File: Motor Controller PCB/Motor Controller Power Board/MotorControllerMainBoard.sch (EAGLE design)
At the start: 51 parts, among them U1 CDBA340L-G

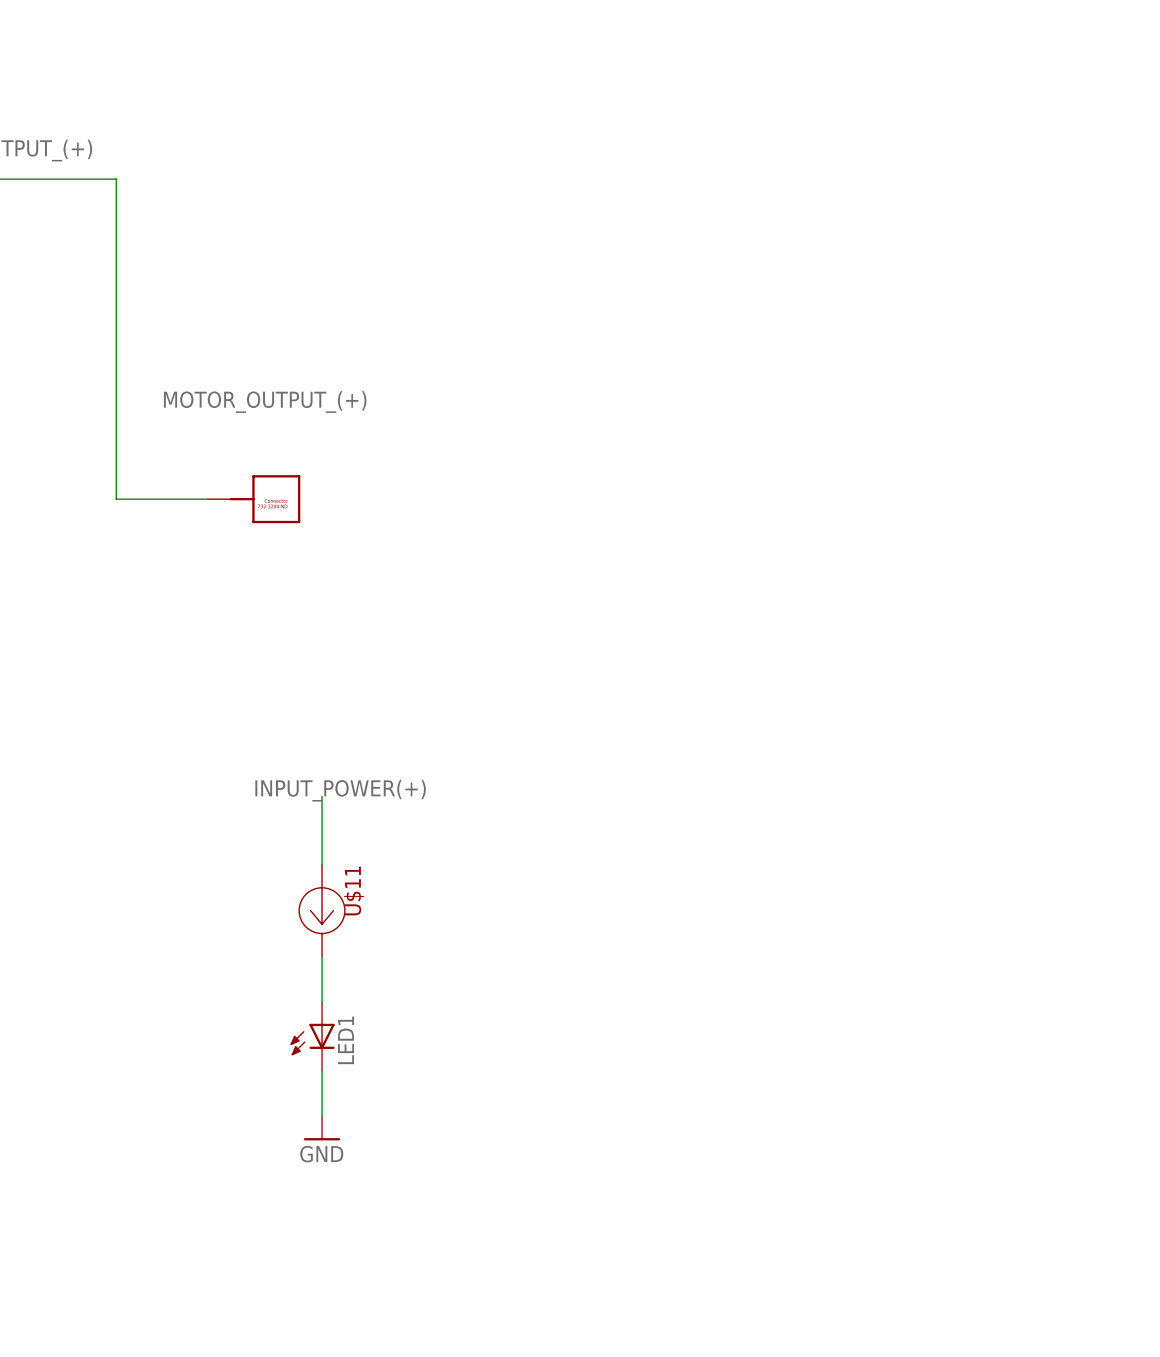
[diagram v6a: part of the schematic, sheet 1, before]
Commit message: Added headers, selected resistor for fet driver
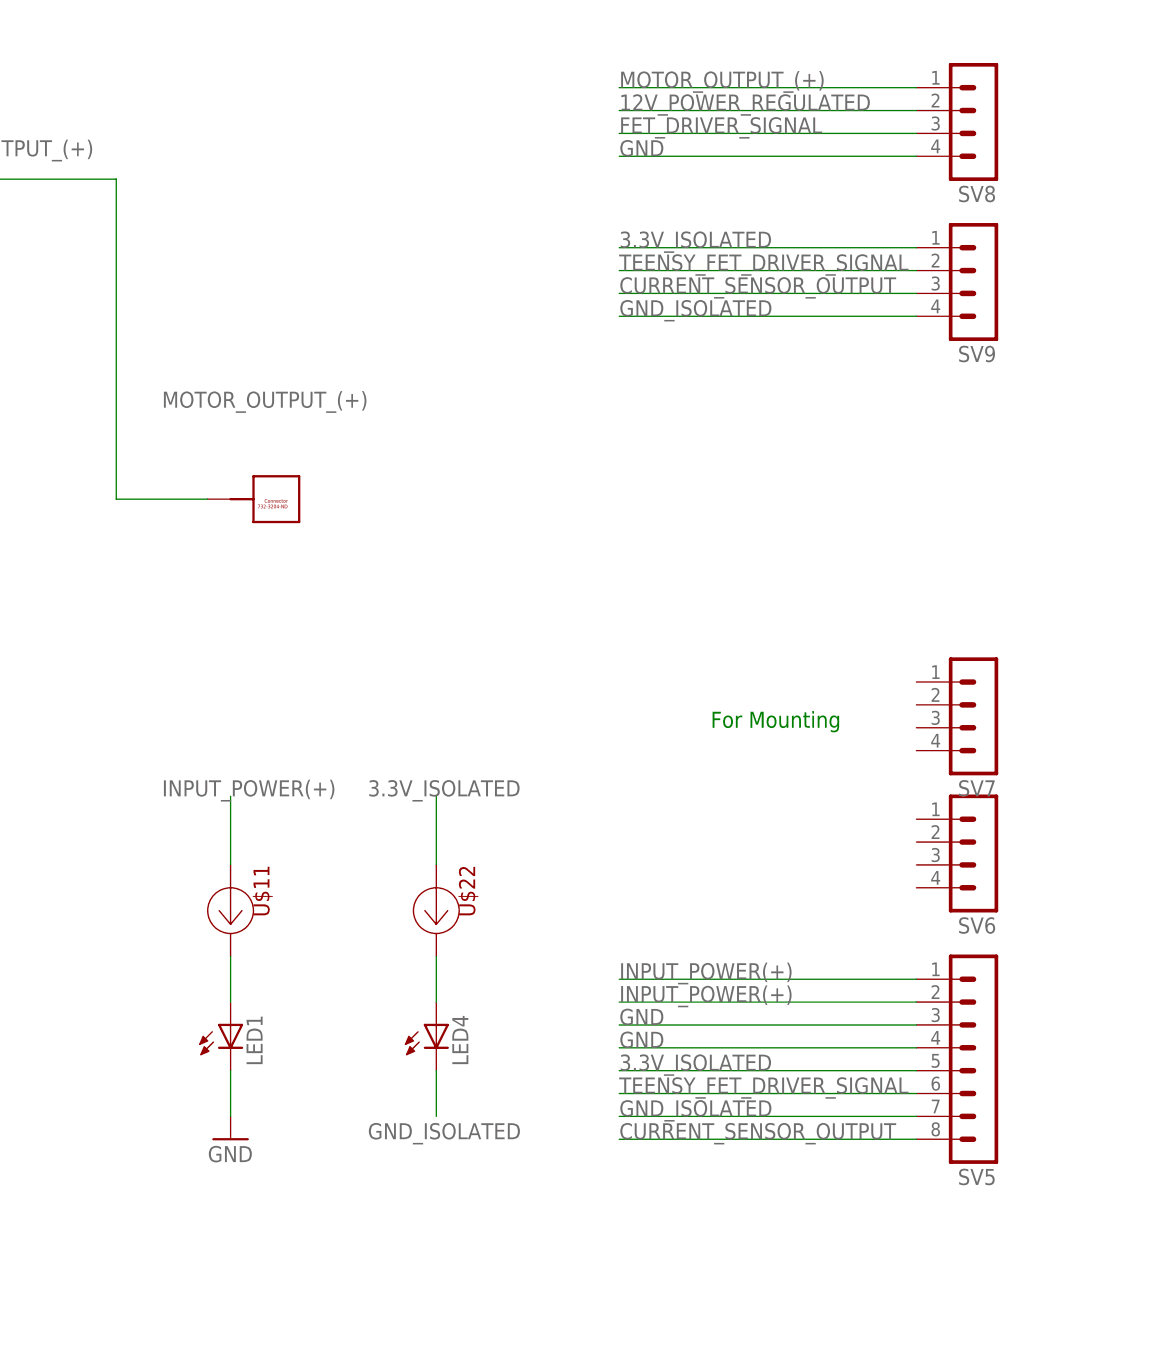
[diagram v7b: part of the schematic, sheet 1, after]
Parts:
- added LED4: (no value), led:LEDCHIPLED_1206
- added SV5: (no value), con-lstb:MA08-1
- added SV6, SV7, SV8, SV9: (no value), con-lstb:MA04-1
- added U$22: (no value), MotorControllerEagleLibrary:AL5809-20S1-7
- R1: value 4.7k -> 332
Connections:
- removed net 3.3V_POWER_REGULATED: L1.1, LED3.A
- new net 3.3V_ISOLATED: L1.1, LED3.A, SV5.5, SV9.1, U$22.A
- new net N$14: LED4.A, U$22.C
- new net TEENSY_FET_DRIVER_SIGNAL: SV5.6, SV9.2
- net 12V_POWER_REGULATED: now also SV8.2
- net CURRENT_SENSOR_OUTPUT: now also SV5.8, SV9.3
- net FET_DRIVER_SIGNAL: now also SV8.3
- net GND: now also SV5.3, SV5.4, SV8.4
- net GND_ISOLATED: now also LED4.C, SV5.7, SV9.4
- net INPUT_POWER(+): now also SV5.1, SV5.2
- net MOTOR_OUTPUT_(+): now also SV8.1
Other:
- note added: "For Mounting"
- note added: "~4mA to 6mA (LED Vf 1.5V to 1.9V) maximum 8mA minimum 2mA"
- note removed: "This component needs to be spec'ed"
- moved on the sheet: LED1, U$11
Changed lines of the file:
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@@
 <part name="FRAME3" library="E-P-008-R1.2" deviceset="FRAME_A_L" device=""/>
 <part name="FRAME4" library="E-P-008-R1.2" deviceset="FRAME_A_L" device=""/>
-<part name="R1" library="resistor" library_urn="urn:adsk.eagle:library:348" deviceset="R-US_" device="R0805" package3d_urn="urn:adsk.eagle:package:26059/1" value="4.7k"/>
+<part name="R1" library="resistor" library_urn="urn:adsk.eagle:library:348" deviceset="R-US_" device="R0805" package3d_urn="urn:adsk.eagle:package:26059/1" value="332"/>
 <part name="C1" library="rcl" library_urn="urn:adsk.eagle:library:334" deviceset="C-EU" device="C1210" package3d_urn="urn:adsk.eagle:package:23619/2" value="22uF"/>
 <part name="C2" library="rcl" library_urn="urn:adsk.eagle:library:334" deviceset="C-EU" device="C0805" package3d_urn="urn:adsk.eagle:package:23617/2" value="2.2uF"/>
@@
 <part name="LED3" library="SparkFun (2015_10_14 22_27_04 UTC)" deviceset="LED" device="1206"/>
 <part name="U$21" library="MotorControllerEagleLibrary" deviceset="AL5809-20S1-7" device=""/>
+<part name="SV5" library="con-lstb" library_urn="urn:adsk.eagle:library:162" deviceset="MA08-1" device="" package3d_urn="urn:adsk.eagle:package:8343/1"/>
+<part name="SV6" library="con-lstb" library_urn="urn:adsk.eagle:library:162" deviceset="MA04-1" device="" package3d_urn="urn:adsk.eagle:package:8337/1"/>
+<part name="SV7" library="con-lstb" library_urn="urn:adsk.eagle:library:162" deviceset="MA04-1" device="" package3d_urn="urn:adsk.eagle:package:8337/1"/>
+<part name="SV8" library="con-lstb" library_urn="urn:adsk.eagle:library:162" deviceset="MA04-1" device="" package3d_urn="urn:adsk.eagle:package:8337/1"/>
+<part name="SV9" library="con-lstb" library_urn="urn:adsk.eagle:library:162" deviceset="MA04-1" device="" package3d_urn="urn:adsk.eagle:package:8337/1"/>
+<part name="U$22" library="MotorControllerEagleLibrary" deviceset="AL5809-20S1-7" device=""/>
+<part name="LED4" library="led" library_urn="urn:adsk.eagle:library:259" deviceset="LED" device="CHIPLED_1206" package3d_urn="urn:adsk.eagle:package:15823/1"/>
 </parts>
 <sheets>
@@
 <text x="175.26" y="25.4" size="2.286" layer="94">Keep it looking neat. Use other sheets to make complicated circuits</text>
 <text x="20.32" y="58.42" size="1.778" layer="91">Terminal Block (Negative)</text>
+<text x="236.22" y="121.92" size="1.778" layer="91">For Mounting</text>
 </plain>
 <instances>
@@
 <instance part="U$15" gate="G$1" x="187.96" y="147.32" rot="R180"/>
 <instance part="U$16" gate="G$1" x="15.24" y="106.68"/>
-<instance part="U$11" gate="G$1" x="193.04" y="101.6" rot="R180"/>
-<instance part="LED1" gate="G$1" x="193.04" y="88.9"/>
-<instance part="GND22" gate="1" x="193.04" y="76.2"/>
+<instance part="U$11" gate="G$1" x="182.88" y="101.6" rot="R180"/>
+<instance part="LED1" gate="G$1" x="182.88" y="88.9"/>
+<instance part="GND22" gate="1" x="182.88" y="76.2"/>
+<instance part="SV5" gate="1" x="266.7" y="86.36" rot="R180"/>
+<instance part="SV6" gate="1" x="266.7" y="106.68" rot="R180"/>
+<instance part="SV7" gate="1" x="266.7" y="121.92" rot="R180"/>
+<instance part="SV8" gate="1" x="266.7" y="187.96" rot="R180"/>
+<instance part="SV9" gate="1" x="266.7" y="170.18" rot="R180"/>
+<instance part="U$22" gate="G$1" x="205.74" y="101.6" rot="R180"/>
+<instance part="LED4" gate="G$1" x="205.74" y="88.9"/>
 </instances>
 <busses>
@@
 </segment>
 <segment>
-<wire x1="193.04" y1="114.3" x2="193.04" y2="106.68" width="0.1524" layer="91"/>
+<wire x1="182.88" y1="114.3" x2="182.88" y2="106.68" width="0.1524" layer="91"/>
 <pinref part="U$11" gate="G$1" pin="A"/>
-<label x="185.42" y="114.3" size="1.778" layer="95"/>
+<label x="175.26" y="114.3" size="1.778" layer="95"/>
+</segment>
+<segment>
+<wire x1="259.08" y1="93.98" x2="226.06" y2="93.98" width="0.1524" layer="91"/>
+<pinref part="SV5" gate="1" pin="1"/>
+<label x="226.06" y="93.98" size="1.778" layer="95"/>
+</segment>
+<segment>
+<wire x1="259.08" y1="91.44" x2="226.06" y2="91.44" width="0.1524" layer="91"/>
+<pinref part="SV5" gate="1" pin="2"/>
+<label x="226.06" y="91.44" size="1.778" layer="95"/>
 </segment>
 </net>
@@
 <segment>
 <pinref part="LED1" gate="G$1" pin="C"/>
-<wire x1="193.04" y1="83.82" x2="193.04" y2="78.74" width="0.1524" layer="91"/>
+<wire x1="182.88" y1="83.82" x2="182.88" y2="78.74" width="0.1524" layer="91"/>
 <pinref part="GND22" gate="1" pin="GND"/>
+</segment>
+<segment>
+<wire x1="259.08" y1="88.9" x2="226.06" y2="88.9" width="0.1524" layer="91"/>
+<pinref part="SV5" gate="1" pin="3"/>
+<label x="226.06" y="88.9" size="1.778" layer="95"/>
+</segment>
+<segment>
+<wire x1="259.08" y1="86.36" x2="226.06" y2="86.36" width="0.1524" layer="91"/>
+<pinref part="SV5" gate="1" pin="4"/>
+<label x="226.06" y="86.36" size="1.778" layer="95"/>
+</segment>
+<segment>
+<pinref part="SV8" gate="1" pin="4"/>
+<wire x1="259.08" y1="185.42" x2="226.06" y2="185.42" width="0.1524" layer="91"/>
+<label x="226.06" y="185.42" size="1.778" layer="95"/>
 </segment>
 </net>
@@
 <wire x1="106.68" y1="104.14" x2="106.68" y2="73.66" width="0.1524" layer="91"/>
 </segment>
+<segment>
+<pinref part="SV8" gate="1" pin="3"/>
+<wire x1="259.08" y1="187.96" x2="226.06" y2="187.96" width="0.1524" layer="91"/>
+<label x="226.06" y="187.96" size="1.778" layer="95"/>
+</segment>
 </net>
 <net name="12V_POWER_REGULATED" class="0">
@@
 <label x="68.58" y="58.42" size="1.778" layer="95"/>
 </segment>
+<segment>
+<pinref part="SV8" gate="1" pin="2"/>
+<wire x1="259.08" y1="190.5" x2="226.06" y2="190.5" width="0.1524" layer="91"/>
+<label x="226.06" y="190.5" size="1.778" layer="95"/>
+</segment>
 </net>
 <net name="TEENSY_FET_DRIVER_SIGNAL" class="0">
@@
 <wire x1="119.38" y1="66.04" x2="119.38" y2="58.42" width="0.1524" layer="91"/>
 <label x="121.92" y="58.42" size="1.778" layer="95"/>
+</segment>
+<segment>
+<wire x1="226.06" y1="81.28" x2="259.08" y2="81.28" width="0.1524" layer="91"/>
+<pinref part="SV5" gate="1" pin="6"/>
+<label x="226.06" y="81.28" size="1.778" layer="95"/>
+</segment>
+<segment>
+<pinref part="SV9" gate="1" pin="2"/>
+<wire x1="259.08" y1="172.72" x2="226.06" y2="172.72" width="0.1524" layer="91"/>
+<label x="226.06" y="172.72" size="1.778" layer="95"/>
 </segment>
 </net>
@@
 <pinref part="U$15" gate="G$1" pin="P$1"/>
 </segment>
+<segment>
+<pinref part="SV8" gate="1" pin="1"/>
+<wire x1="259.08" y1="193.04" x2="226.06" y2="193.04" width="0.1524" layer="91"/>
+<label x="226.06" y="193.04" size="1.778" layer="95"/>
+</segment>
 </net>
 <net name="N$17" class="0">
@@
 <pinref part="U$11" gate="G$1" pin="C"/>
 <pinref part="LED1" gate="G$1" pin="A"/>
-<wire x1="193.04" y1="96.52" x2="193.04" y2="91.44" width="0.1524" layer="91"/>
+<wire x1="182.88" y1="96.52" x2="182.88" y2="91.44" width="0.1524" layer="91"/>
+</segment>
+</net>
+<net name="GND_ISOLATED" class="0">
+<segment>
+<pinref part="SV5" gate="1" pin="7"/>
+<wire x1="259.08" y1="78.74" x2="226.06" y2="78.74" width="0.1524" layer="91"/>
+<label x="226.06" y="78.74" size="1.778" layer="95"/>
+</segment>
+<segment>
+<pinref part="SV9" gate="1" pin="4"/>
+<wire x1="259.08" y1="167.64" x2="226.06" y2="167.64" width="0.1524" layer="91"/>
+<label x="226.06" y="167.64" size="1.778" layer="95"/>
+</segment>
+<segment>
+<pinref part="LED4" gate="G$1" pin="C"/>
+<wire x1="205.74" y1="83.82" x2="205.74" y2="78.74" width="0.1524" layer="91"/>
+<label x="198.12" y="76.2" size="1.778" layer="95"/>
+</segment>
+</net>
+<net name="3.3V_ISOLATED" class="0">
+<segment>
+<wire x1="259.08" y1="83.82" x2="226.06" y2="83.82" width="0.1524" layer="91"/>
+<pinref part="SV5" gate="1" pin="5"/>
+<label x="226.06" y="83.82" size="1.778" layer="95"/>
+</segment>
+<segment>
+<pinref part="SV9" gate="1" pin="1"/>
+<wire x1="259.08" y1="175.26" x2="226.06" y2="175.26" width="0.1524" layer="91"/>
+<label x="226.06" y="175.26" size="1.778" layer="95"/>
+</segment>
+<segment>
+<wire x1="205.74" y1="114.3" x2="205.74" y2="106.68" width="0.1524" layer="91"/>
+<pinref part="U$22" gate="G$1" pin="A"/>
+<label x="198.12" y="114.3" size="1.778" layer="95"/>
+</segment>
+</net>
+<net name="CURRENT_SENSOR_OUTPUT" class="0">
+<segment>
+<pinref part="SV5" gate="1" pin="8"/>
+<wire x1="259.08" y1="76.2" x2="226.06" y2="76.2" width="0.1524" layer="91"/>
+<label x="226.06" y="76.2" size="1.778" layer="95"/>
+</segment>
+<segment>
+<pinref part="SV9" gate="1" pin="3"/>
+<wire x1="259.08" y1="170.18" x2="226.06" y2="170.18" width="0.1524" layer="91"/>
+<label x="226.06" y="170.18" size="1.778" layer="95"/>
+</segment>
+</net>
+<net name="N$14" class="0">
+<segment>
+<pinref part="U$22" gate="G$1" pin="C"/>
+<pinref part="LED4" gate="G$1" pin="A"/>
+<wire x1="205.74" y1="96.52" x2="205.74" y2="91.44" width="0.1524" layer="91"/>
 </segment>
 </net>
@@
 <text x="193.04" y="27.94" size="5.08" layer="94">MOSFET DRIVER</text>
 <text x="149.86" y="142.24" size="1.778" layer="94">All must be X7R</text>
-<text x="104.14" y="99.06" size="1.778" layer="92">This component
-needs to be
-spec'ed </text>
+<text x="86.36" y="96.52" size="1.778" layer="92">~4mA to 6mA
+(LED Vf 1.5V to 1.9V)
+maximum 8mA
+minimum 2mA</text>
 </plain>
 <instances>
@@
 </segment>
 </net>
-<net name="3.3V_POWER_REGULATED" class="0">
+<net name="3.3V_ISOLATED" class="0">
 <segment>
 <pinref part="L1" gate="G$1" pin="1"/>
